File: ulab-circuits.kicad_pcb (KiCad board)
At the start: 2 copper layers, 40 parts, among them J1 Conn_01x01_Female, Q1 BC547, U1 LM555, U2 LM555

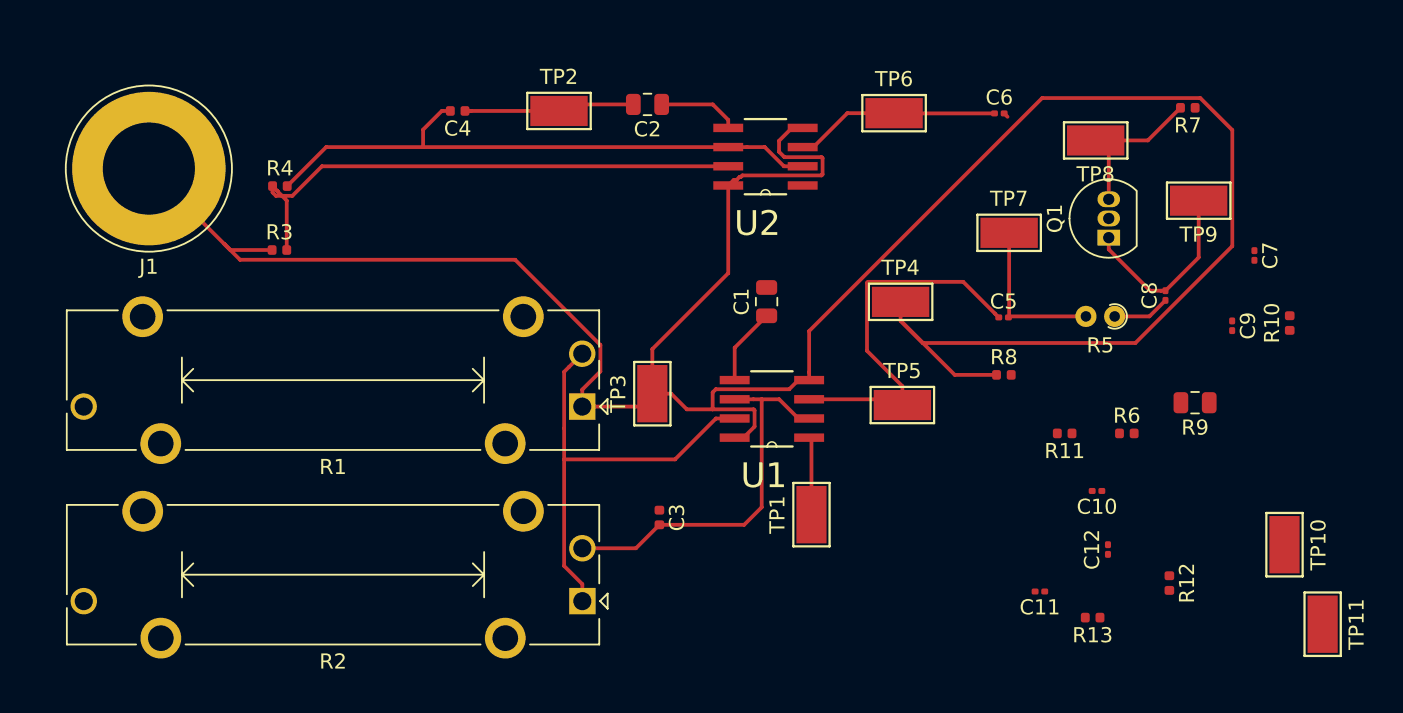
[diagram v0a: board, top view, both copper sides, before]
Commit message: layout done except grounds and +10Vs
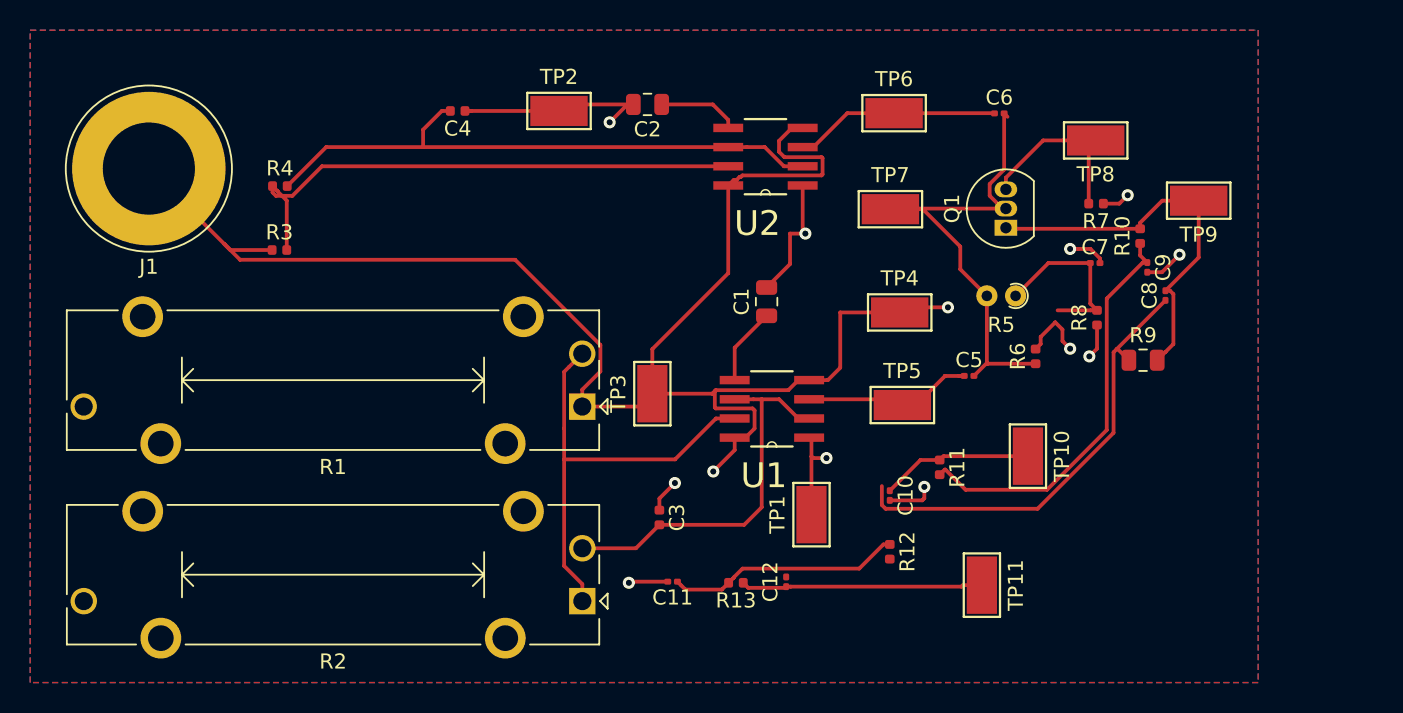
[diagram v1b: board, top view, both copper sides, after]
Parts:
- moved C11 24.3 mm to (200.0, 100.0)
- moved R13 23.7 mm to (204.2, 100.1)
- moved TP11 22.7 mm to (220.5, 100.2)
- moved C12 21.4 mm to (207.5, 100.0)
- moved R12 18.6 mm to (214.4, 98.0)
- moved TP10 18.0 mm to (223.5, 91.7)
- moved C10 13.7 mm to (214.4, 94.3), turned to 270 degrees
- moved R10 11.5 mm to (230.9, 77.1)
- moved C7 10.6 mm to (228.0, 78.9), turned to 0 degrees
- moved R7 8.78 mm to (228.0, 75.0)
- moved R11 8.57 mm to (217.7, 92.4), turned to 270 degrees
- moved TP7 8.01 mm to (214.4, 75.3)
- moved R6 7.90 mm to (224.0, 85.1), turned to 90 degrees
- moved R8 7.24 mm to (228.1, 82.5), turned to 90 degrees
- moved Q1 6.84 mm to (222.1, 76.6)
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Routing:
- net +10V: track 176.3 -> 114.5 mm, vias 0 -> 3
- net Net-(C7-Pad1): track 3.80 -> 41.8 mm
- net GND: track 16.7 -> 47.7 mm, vias 0 -> 10
- net Net-(C9-Pad1): track 0.00 -> 27.2 mm
- net Net-(C5-Pad2): track 11.1 -> 33.8 mm
- net Net-(C12-Pad1): track 0.00 -> 16.0 mm
- net Net-(C11-Pad1): track 0.00 -> 15.5 mm
- net /var_oscillator: track 25.1 -> 11.2 mm
- net Net-(C8-Pad2): track 12.5 -> 26.3 mm
- net Net-(C10-Pad1): track 0.00 -> 10.1 mm
- net Net-(Q1-Pad3): track 10.8 -> 13.3 mm
- added copper zone on B.Cu, net +10V
- added copper zone on F.Cu, net GND

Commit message: passed DRC
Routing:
- net GND: track 47.7 -> 173.7 mm, vias 10 -> 14
- net Net-(C7-Pad1): track 41.8 -> 18.3 mm
- net Net-(C9-Pad1): track 27.2 -> 45.8 mm
- net +10V: track 114.5 -> 125.3 mm
- net Net-(C8-Pad2): track 26.3 -> 36.3 mm
- net Net-(C10-Pad1): track 10.1 -> 15.9 mm
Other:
- net class Default: clearance 0.2 -> 0.1524; trace_width 0.25 -> 0.2; via_dia 0.8 -> 0.6858; via_drill 0.4 -> 0.3302
- rule trace_clearance: 0.2 -> 0.1524
